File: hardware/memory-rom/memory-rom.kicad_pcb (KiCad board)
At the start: 2 copper layers, 77 x 39 mm, 26 parts, among them J1 Conn_Mem_Ext, J2 Conn_Power, U1 SST39VF040-70-4C-NHE, U2 74LVC1G86, U3 74LVC1G32, U4 74LVC1G332, U5 74LVC1G86, U6 MIC5504-3.3YM5

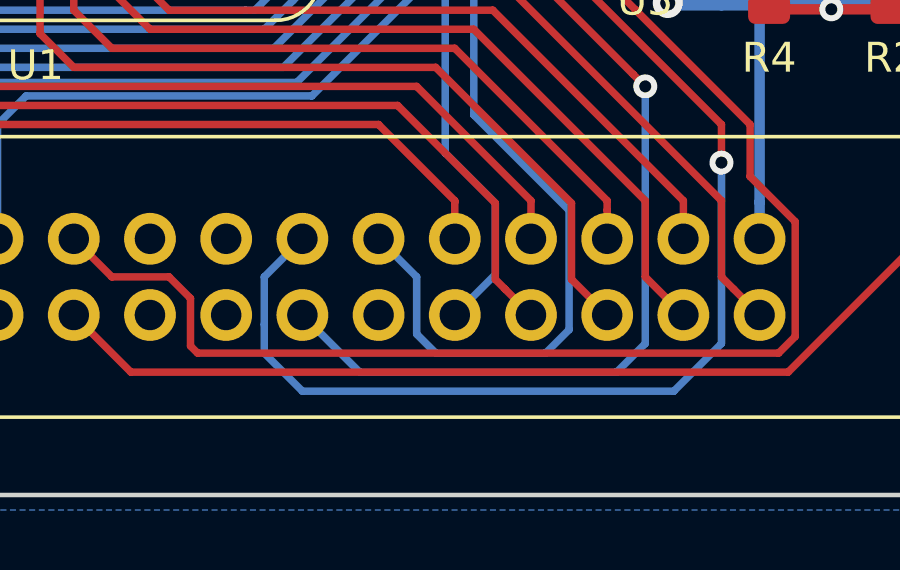
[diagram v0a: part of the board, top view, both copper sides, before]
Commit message: Added ~RESET to memory bus
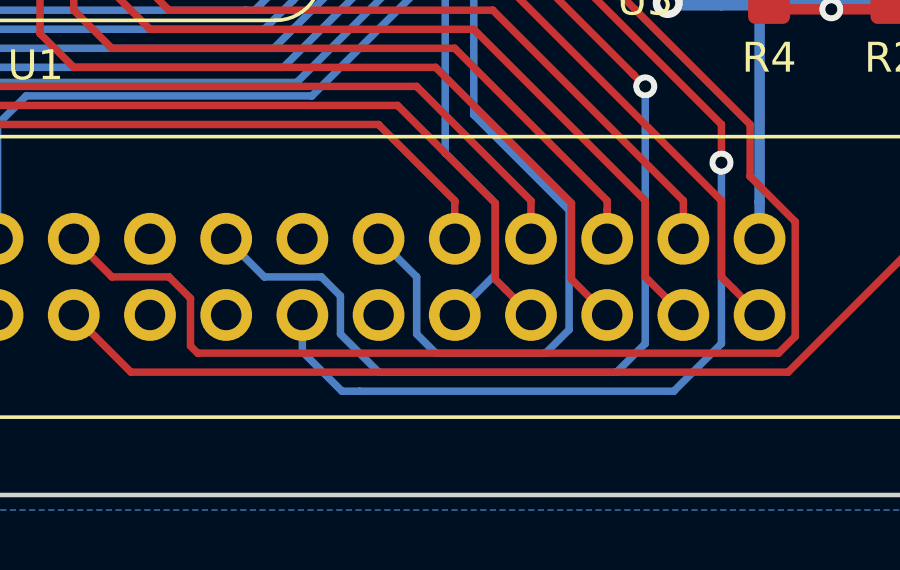
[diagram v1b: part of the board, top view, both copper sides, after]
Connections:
- J1 pad 26: /A24 -> /A30
- J1 pad 27: /A30 -> /A31
- J1 pad 28: /A31 -> /~RESET
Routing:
- net /A31: track 46.4 -> 42.1 mm
- net /A30: track 38.0 -> 42.3 mm
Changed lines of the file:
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@@
     (thickness 1.6)
     (drawings 15)
-    (tracks 535)
+    (tracks 538)
     (zones 0)
     (modules 26)
@@
   )
   (setup
-    (last_trace_width 0.35)
+    (last_trace_width 0.25)
     (user_trace_width 0.35)
     (user_trace_width 0.5)
@@
     (solder_mask_min_width 0.25)
     (aux_axis_origin 0 0)
-    (grid_origin 67 98)
+    (grid_origin 107.8275 124.46)
     (visible_elements FFFDFF7F)
     (pcbplotparams
@@
   (net 47 /A22)
   (net 48 /A23)
-  (net 49 /A24)
+  (net 49 /~RESET)
   (net_class Default "This is the default net class."
     (clearance 0.2)
@@
     (add_net /A22)
     (add_net /A23)
-    (add_net /A24)
     (add_net /A3)
     (add_net /A30)
@@
     (add_net /~MEM_OE)
     (add_net /~MEM_WE)
+    (add_net /~RESET)
     (add_net /~WAIT)
     (add_net GND)
@@
       (net 48 /A23))
     (pad 26 thru_hole oval (at 2.54 30.48 90) (size 1.7272 1.7272) (drill 1.016) (layers *.Cu *.Mask)
-      (net 49 /A24))
+      (net 5 /A30))
     (pad 27 thru_hole oval (at 0 33.02 90) (size 1.7272 1.7272) (drill 1.016) (layers *.Cu *.Mask)
-      (net 5 /A30))
+      (net 4 /A31))
     (pad 28 thru_hole oval (at 2.54 33.02 90) (size 1.7272 1.7272) (drill 1.016) (layers *.Cu *.Mask)
-      (net 4 /A31))
+      (net 49 /~RESET))
     (pad 29 thru_hole oval (at 0 35.56 90) (size 1.7272 1.7272) (drill 1.016) (layers *.Cu *.Mask)
       (net 35 /~WAIT))
@@
   (segment (start 128 102.8) (end 126.5625 102.8) (width 0.35) (layer B.Cu) (net 3))
   (segment (start 118.6225 100.6475) (end 117.1075 100.6475) (width 0.35) (layer B.Cu) (net 3))
-  (segment (start 110.3675 124.46) (end 109.0975 125.73) (width 0.25) (layer B.Cu) (net 4))
-  (segment (start 109.0975 125.73) (end 109.0975 127.3175) (width 0.25) (layer B.Cu) (net 4))
-  (segment (start 109.0975 127.3175) (end 109.0975 128.27) (width 0.25) (layer B.Cu) (net 4))
-  (segment (start 109.0975 128.27) (end 110.3675 129.54) (width 0.25) (layer B.Cu) (net 4))
-  (segment (start 110.3675 129.54) (end 122.75 129.54) (width 0.25) (layer B.Cu) (net 4))
   (segment (start 122.75 129.54) (end 124.3375 127.9525) (width 0.25) (layer B.Cu) (net 4))
   (via (at 124.3375 121.92) (size 0.8) (drill 0.4) (layers F.Cu B.Cu) (net 4))
@@
   (segment (start 117.9875 106.3625) (end 117.9875 114.3) (width 0.25) (layer F.Cu) (net 4))
   (segment (start 124.3375 120.65) (end 118.6225 114.935) (width 0.25) (layer F.Cu) (net 4))
-  (segment (start 110.3675 127) (end 112.2725 128.905) (width 0.25) (layer B.Cu) (net 5))
-  (segment (start 112.2725 128.905) (end 120.845 128.905) (width 0.25) (layer B.Cu) (net 5))
+  (segment (start 111.686186 129.54) (end 112.2725 129.54) (width 0.25) (layer B.Cu) (net 4))
+  (segment (start 110.3675 128.221314) (end 111.686186 129.54) (width 0.25) (layer B.Cu) (net 4))
+  (segment (start 110.3675 127) (end 110.3675 128.221314) (width 0.25) (layer B.Cu) (net 4))
+  (segment (start 112.2725 129.54) (end 122.75 129.54) (width 0.25) (layer B.Cu) (net 4))
   (segment (start 120.845 128.905) (end 121.7975 127.9525) (width 0.25) (layer B.Cu) (net 5))
   (via (at 121.7975 119.38) (size 0.8) (drill 0.4) (layers F.Cu B.Cu) (net 5))
@@
   (segment (start 116.085 106.36) (end 116.0825 106.3625) (width 0.25) (layer B.Cu) (net 5))
   (segment (start 116.085 104.9225) (end 116.085 106.36) (width 0.25) (layer B.Cu) (net 5))
+  (segment (start 111.6375 127.635) (end 112.9075 128.905) (width 0.25) (layer B.Cu) (net 5))
+  (segment (start 112.9075 128.905) (end 120.845 128.905) (width 0.25) (layer B.Cu) (net 5))
+  (segment (start 111.6375 126.365) (end 111.6375 127.635) (width 0.25) (layer B.Cu) (net 5))
+  (segment (start 107.8275 124.46) (end 109.0975 125.73) (width 0.25) (layer B.Cu) (net 5))
+  (segment (start 109.0975 125.73) (end 111.0025 125.73) (width 0.25) (layer B.Cu) (net 5))
+  (segment (start 111.0025 125.73) (end 111.6375 126.365) (width 0.25) (layer B.Cu) (net 5))
   (segment (start 104.0175 99.455002) (end 103.142502 100.33) (width 0.25) (layer F.Cu) (net 6))
   (segment (start 104.0175 98.425) (end 104.0175 99.455002) (width 0.25) (layer F.Cu) (net 6))

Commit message: Unified footprints
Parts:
- D1: footprint LED_SMD:LED_0805_2012Metric -> LED_SMD:LED_0805_2012Metric_Pad1.15x1.40mm_HandSolder
- R1, R2, R3, R4, R5: footprint Resistor_SMD:R_0805_2012Metric -> Resistor_SMD:R_0805_2012Metric_Pad1.15x1.40mm_HandSolder
- U2, U3, U5, U6: footprint Package_TO_SOT_SMD:SOT-23-5 -> Package_TO_SOT_SMD:SOT-23-5_HandSoldering
- U4: footprint Package_TO_SOT_SMD:SOT-23-6 -> Package_TO_SOT_SMD:SOT-23-6_Handsoldering
- moved C2 1.16 mm to (120.8, 114.0)
- moved U6 0.61 mm to (124.5, 114.0)
- moved C6 0.55 mm to (116.1, 100.1)
- moved C8 0.39 mm to (121.9, 110.1)
- moved R1 0.09 mm to (130.0, 113.9)
- moved R3 0.09 mm to (125.9, 113.9)
- moved R2 0.09 mm to (130.0, 116.0)
- moved R4 0.09 mm to (125.9, 116.0)
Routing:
- net VCC: track 127.7 -> 132.9 mm, vias 6 -> 7
- net Net-(D1-Pad1): track 2.55 -> 3.66 mm
- net GND: track 161.6 -> 162.7 mm, vias 5 -> 6
- net /V_IN: track 9.30 -> 10.3 mm
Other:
- board text added: "2020-06-11"
- board text removed: "2020-05-30"
